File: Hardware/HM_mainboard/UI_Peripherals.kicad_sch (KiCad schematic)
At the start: 16 parts, among them J4 54-00174, J5 54-00174, J6 54-00174, J7 54-00174, U4 WE-TVS-824015043

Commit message: Updated BOM
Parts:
- C6: Digikey 1276-CL10B104KB8NNNLCT -> 1276-CL10B104KB8NNNLCT-ND
- D3, D4: Mouser 710-155124RV73200 -> 155124RV73200
- J4, J5, J6, J7: Digikey 839-54-00174CT -> 54-00174
- R6: Mouser 603-RC0603FR-10120RL -> ERJ-PA3J121V
- S3: Mouser 710-450404015514 -> 450404015514
- U4: Mouser 710-824015043 -> 824015043
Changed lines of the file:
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@@
       (effects (font (size 1.27 1.27)) hide)
     )
-    (property "Mouser" "710-155124RV73200" (at 120.65 137.16 0)
+    (property "Mouser" "155124RV73200" (at 120.65 137.16 0)
       (effects (font (size 1.27 1.27)) hide)
     )
@@
       (effects (font (size 1.27 1.27)) hide)
     )
-    (property "Mouser" "710-824015043" (at 246.38 137.16 0)
+    (property "Mouser" "824015043" (at 246.38 137.16 0)
       (effects (font (size 1.27 1.27)) hide)
     )
@@
       (effects (font (size 1.27 1.27)) hide)
     )
-    (property "Mouser" "603-RC0603FR-10120RL" (at 118.11 153.67 0)
+    (property "Mouser" "ERJ-PA3J121V" (at 118.11 153.67 0)
       (effects (font (size 1.27 1.27)) hide)
     )
@@
       (effects (font (size 1.27 1.27)) (justify left top) hide)
     )
-    (property "Mouser" "710-450404015514" (at 179.07 130.81 0)
+    (property "Mouser" "450404015514" (at 179.07 130.81 0)
       (effects (font (size 1.27 1.27)) hide)
     )
@@
       (effects (font (size 1.27 1.27) italic) hide)
     )
-    (property "Digikey" "839-54-00174CT" (at 233.68 50.8 0)
+    (property "Digikey" "54-00174" (at 233.68 50.8 0)
       (effects (font (size 1.27 1.27)) hide)
     )
@@
       (effects (font (size 1.27 1.27)) hide)
     )
-    (property "Mouser" "603-RC0603FR-10120RL" (at 59.69 152.4 0)
+    (property "Mouser" "ERJ-PA3J121V" (at 59.69 152.4 0)
       (effects (font (size 1.27 1.27)) hide)
     )
@@
       (effects (font (size 1.27 1.27)) hide)
     )
-    (property "Digikey" "1276-CL10B104KB8NNNLCT" (at 123.19 62.23 0)
+    (property "Digikey" "1276-CL10B104KB8NNNLCT-ND" (at 123.19 62.23 0)
       (effects (font (size 1.27 1.27)) hide)
     )
@@
       (effects (font (size 1.27 1.27) italic) hide)
     )
-    (property "Digikey" "839-54-00174CT" (at 172.72 50.8 0)
+    (property "Digikey" "54-00174" (at 172.72 50.8 0)
       (effects (font (size 1.27 1.27)) hide)
     )
@@
       (effects (font (size 1.27 1.27)) hide)
     )
-    (property "Digikey" "1276-CL10B104KB8NNNLCT" (at 243.84 60.96 0)
+    (property "Digikey" "1276-CL10B104KB8NNNLCT-ND" (at 243.84 60.96 0)
       (effects (font (size 1.27 1.27)) hide)
     )
@@
       (effects (font (size 1.27 1.27) italic) hide)
     )
-    (property "Digikey" "839-54-00174CT" (at 113.03 52.07 0)
+    (property "Digikey" "54-00174" (at 113.03 52.07 0)
       (effects (font (size 1.27 1.27)) hide)
     )
@@
       (effects (font (size 1.27 1.27)) hide)
     )
-    (property "Mouser" "603-RC0603FR-10120RL" (at 54.61 152.4 0)
+    (property "Mouser" "ERJ-PA3J121V" (at 54.61 152.4 0)
       (effects (font (size 1.27 1.27)) hide)
     )
@@
       (effects (font (size 1.27 1.27)) hide)
     )
-    (property "Mouser" "603-RC0603FR-10120RL" (at 123.19 153.67 0)
+    (property "Mouser" "ERJ-PA3J121V" (at 123.19 153.67 0)
       (effects (font (size 1.27 1.27)) hide)
     )
@@
       (effects (font (size 1.27 1.27)) hide)
     )
-    (property "Digikey" "1276-CL10B104KB8NNNLCT" (at 62.23 62.23 0)
+    (property "Digikey" "1276-CL10B104KB8NNNLCT-ND" (at 62.23 62.23 0)
       (effects (font (size 1.27 1.27)) hide)
     )
@@
       (effects (font (size 1.27 1.27)) hide)
     )
-    (property "Digikey" "1276-CL10B104KB8NNNLCT" (at 182.88 60.96 0)
+    (property "Digikey" "1276-CL10B104KB8NNNLCT-ND" (at 182.88 60.96 0)
       (effects (font (size 1.27 1.27)) hide)
     )
@@
       (effects (font (size 1.27 1.27)) hide)
     )
-    (property "Mouser" "710-155124RV73200" (at 57.15 137.16 0)
+    (property "Mouser" "155124RV73200" (at 57.15 137.16 0)
       (effects (font (size 1.27 1.27)) hide)
     )
@@
       (effects (font (size 1.27 1.27) italic) hide)
     )
-    (property "Digikey" "839-54-00174CT" (at 52.07 52.07 0)
-      (effects (font (size 1.27 1.27)) hide)
-    )
+    (property "Digikey" "54-00174" (at 52.07 52.07 0)
+      (effects (font (size 1.27 1.27)) hide)
+    )

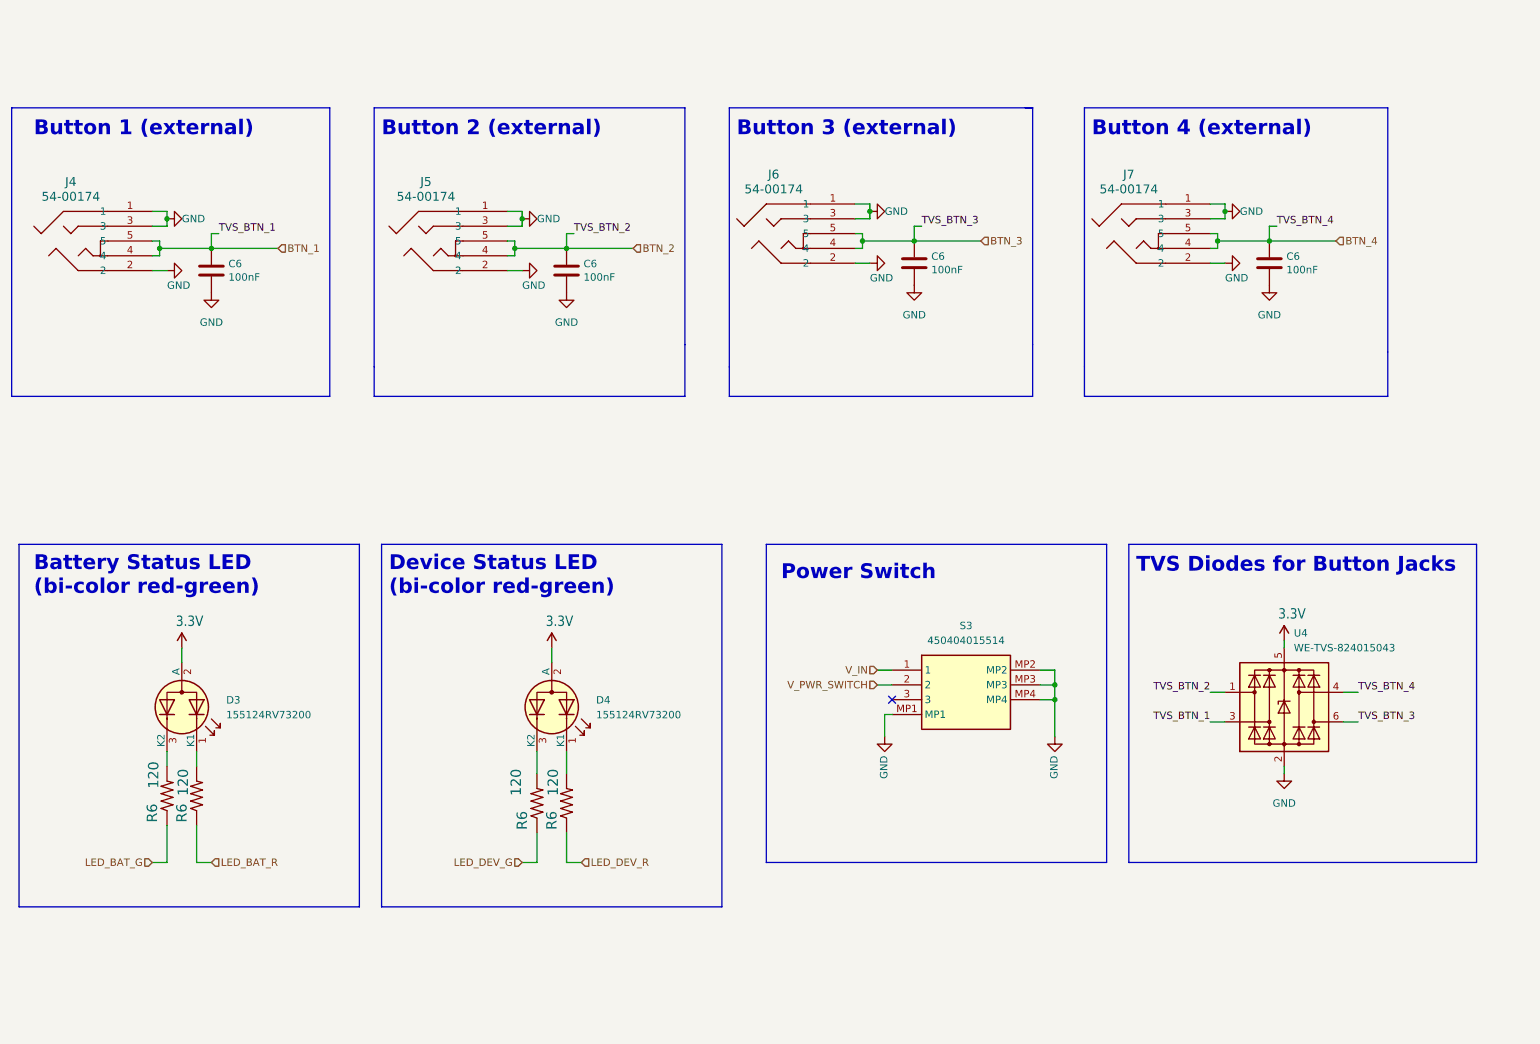
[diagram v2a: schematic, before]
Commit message: Added connector for sip&puff sensor
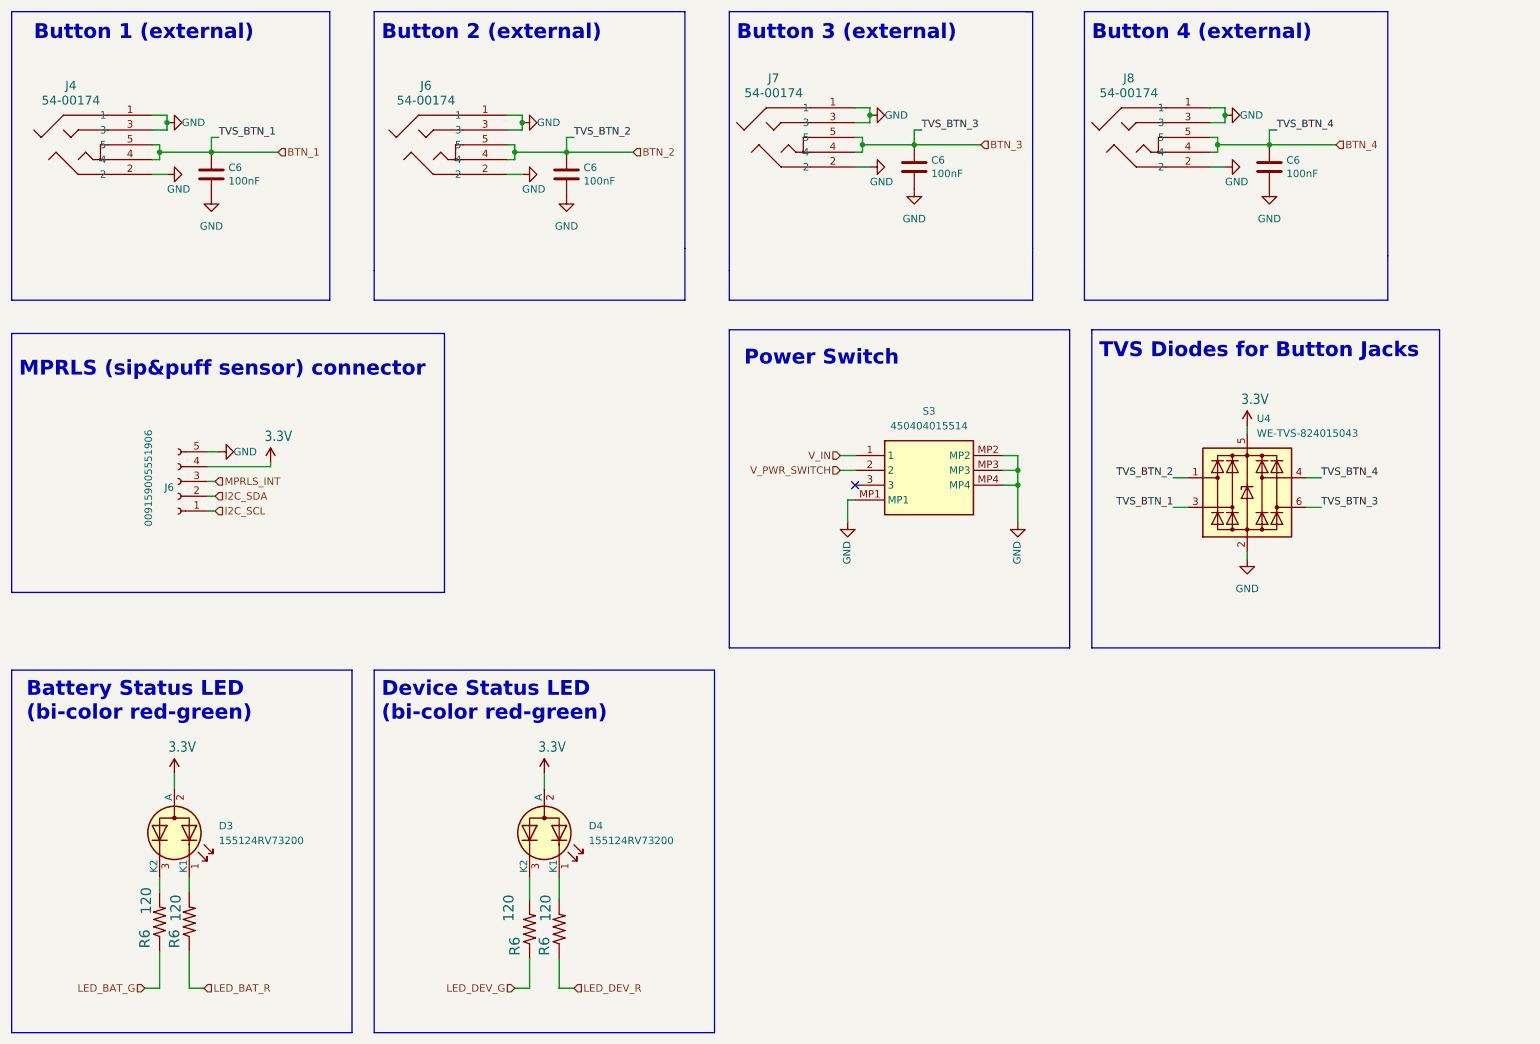
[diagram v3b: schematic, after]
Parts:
- added J6: 009159005551906, HeadMouse:009159005551906, symbol Connector:Conn_01x05_Socket
- renumbered J5 to J6, J6 to J7, J7 to J8
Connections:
- net 3.3V: now also J6.4 (Pin_4)
- net GND: now also J6.5 (Pin_5)
- new net I2C_SCL: J6.1 (Pin_1)
- new net I2C_SDA: J6.2 (Pin_2)
- new net MPRLS_INT: J6.3 (Pin_3)
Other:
- note added: "MPRLS (sip&puff sensor) connector"
- moved on the sheet: C6, D3, D4, J4, J6, J7, J8, R6, S3, U4

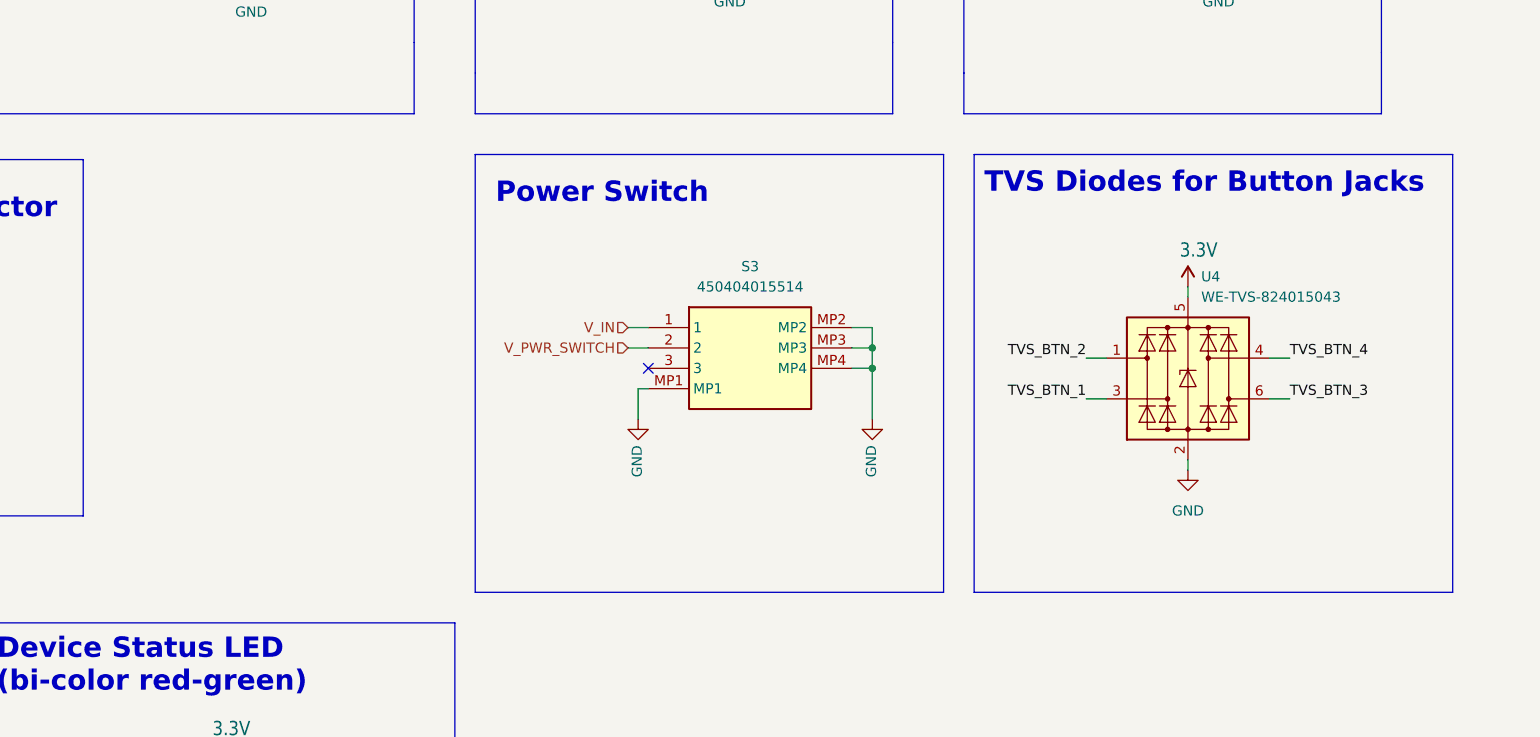
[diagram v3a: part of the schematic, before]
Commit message: Updated schematic to version v2.0.0
•	Removed two 6-Axis IMUs
•	As the BNO055 did not respond to I2C requests, a 2k7 pullup was added in parallel to the I2C-SDA pullup. The behavior is described here:  https://forums.adafruit.com/viewtopic.php?t=205215
•	Added mounting holes for enclosure
•	Added board description prints
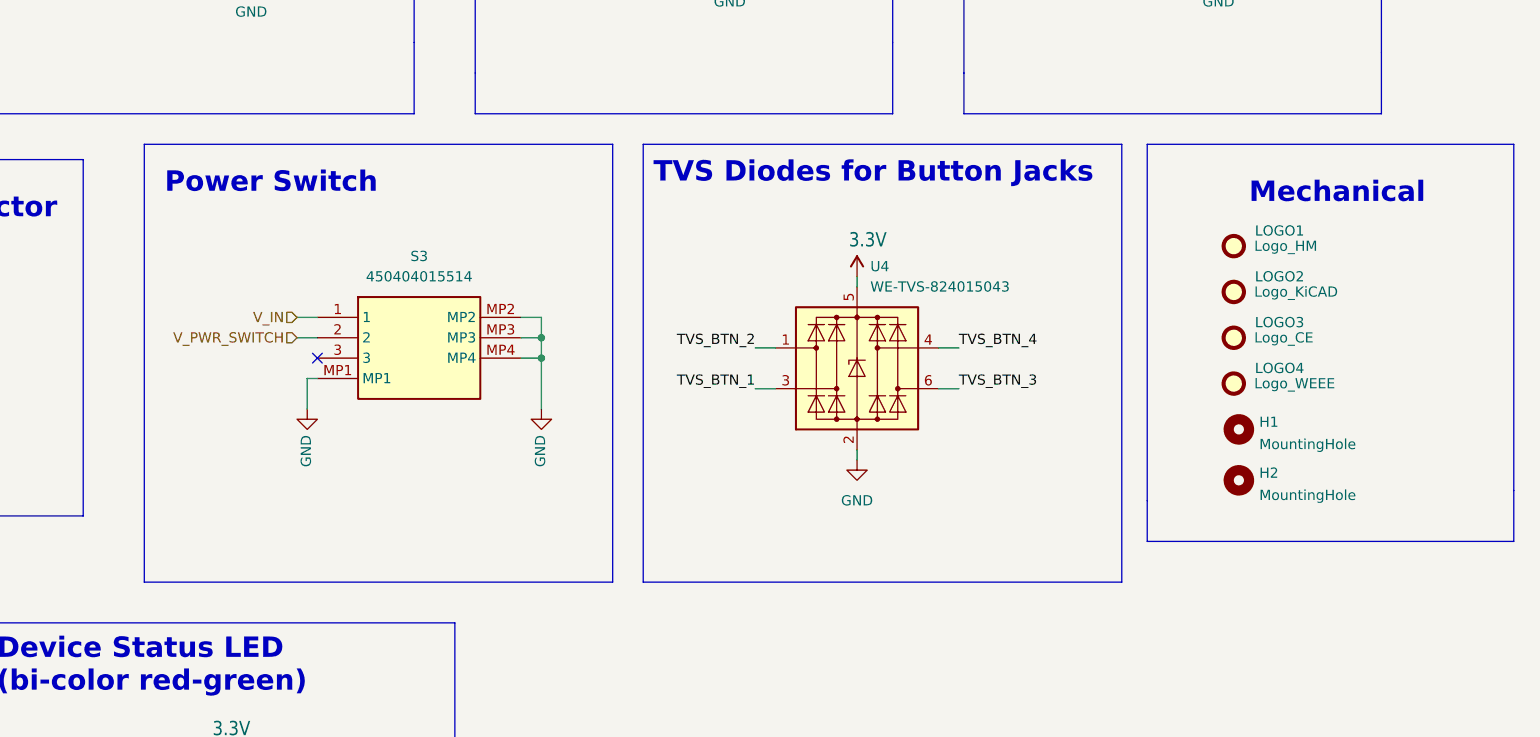
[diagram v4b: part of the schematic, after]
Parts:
- added H1, H2: MountingHole, MountingHole:MountingHole_2.2mm_M2_ISO7380, symbol Mechanical:MountingHole
- added LOGO1: Logo_HM, HeadMouse:LOGO_HM_V2.0.0, symbol HeadMouse:LOGO
- added LOGO2: Logo_KiCAD, Symbol:KiCad-Logo_5mm_SilkScreen, symbol HeadMouse:LOGO
- added LOGO3: Logo_CE, Symbol:CE-Logo_8.5x6mm_SilkScreen, symbol HeadMouse:LOGO
- added LOGO4: Logo_WEEE, Symbol:WEEE-Logo_5.6x8mm_SilkScreen, symbol HeadMouse:LOGO
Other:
- note added: "Mechanical"
- moved on the sheet: S3, U4

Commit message: Added BOM, PDF and zipped V2.0.0 project data
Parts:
- removed J8: 54-00174, HeadMouse:54-00174, symbol HeadMouse:54-00174
- added SW1: SKHHLQA010, Button_Switch_THT:SW_Tactile_SPST_Angled_PTS645Vx58-2LFS, symbol Switch:SW_Push
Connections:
- net BTN_4: now also SW1.2
- net GND: now also SW1.1
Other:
- note added: "Button 4 (BLE/config)"
- note removed: "Button 4 (external)"
